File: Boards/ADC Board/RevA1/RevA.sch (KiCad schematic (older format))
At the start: 3 parts, among them J1 Left Connector, J2 Right Connector, M2.1 CMH

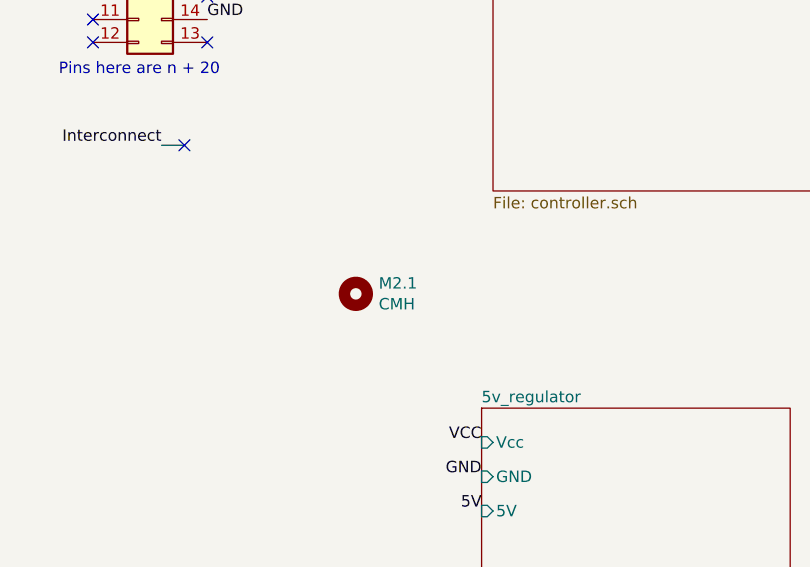
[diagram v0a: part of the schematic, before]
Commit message: Created and layed out most of PCB for microvolt board. Removed one strain module, and added multiple mounting holes for the boards to be placed on.
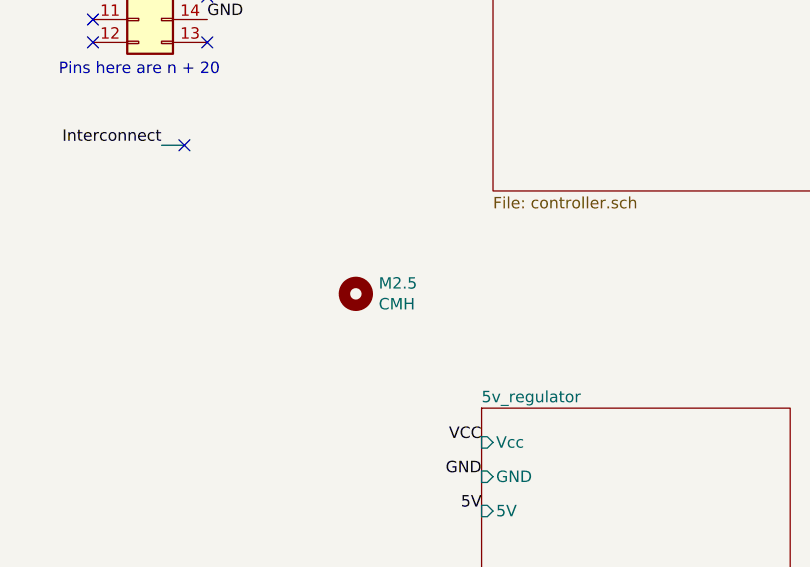
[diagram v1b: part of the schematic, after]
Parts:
- renumbered M2.1 to M2.5
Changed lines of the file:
@@
 I2C_Clock
 $Comp
-L Mechanical:MountingHole M2.1
+L Mechanical:MountingHole M2.5
 U 1 1 616626E5
 P 3950 3550
-F 0 "M2.1" H 4050 3596 50  0000 L CNN
+F 0 "M2.5" H 4050 3596 50  0000 L CNN
 F 1 "CMH" H 4050 3505 50  0000 L CNN
 F 2 "MountingHole:MountingHole_2.7mm_M2.5" H 3950 3550 50  0001 C CNN

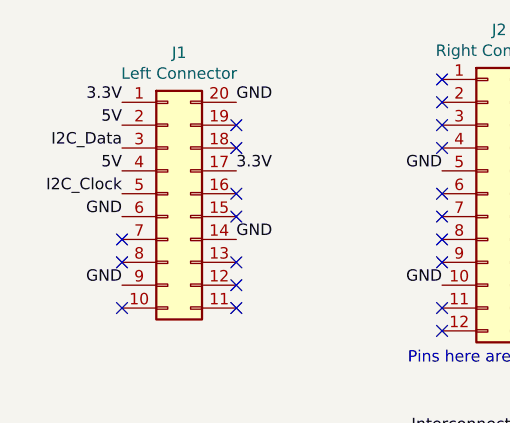
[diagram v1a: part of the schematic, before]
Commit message: In process of updating ADC board to remove 5V connection from PI. Also commiting small changes to uV board.
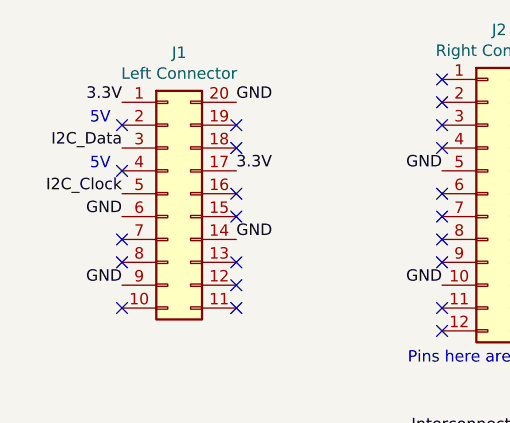
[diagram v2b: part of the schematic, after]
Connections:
- net 5V: no longer J1.2 (Pin_2), J1.4 (Pin_4)
- no-connect marks 27 -> 29
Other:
- note added: "5V"
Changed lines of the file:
@@
 Text Label 1400 1450 2    50   ~ 0
 3.3V
-Text Label 1400 1550 2    50   ~ 0
-5V
-Text Label 1400 1750 2    50   ~ 0
-5V
 Text Label 1400 1950 2    50   ~ 0
 GND
@@
 	3100 2900 3200 2900
 NoConn ~ 3200 2900
+NoConn ~ 1400 1550
+NoConn ~ 1400 1750
+Text Notes 1350 1550 2    50   ~ 0
+5V
+Text Notes 1350 1750 2    50   ~ 0
+5V
 $EndSCHEMATC
